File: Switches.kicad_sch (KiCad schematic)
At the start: 31 parts, among them SW4 SW_SPST, SW5 SW_SPST, SW6 SW_SPST, SW7 SW_SPST, SW8 SW_SPST, SW9 SW_SPST, U4 74HC14

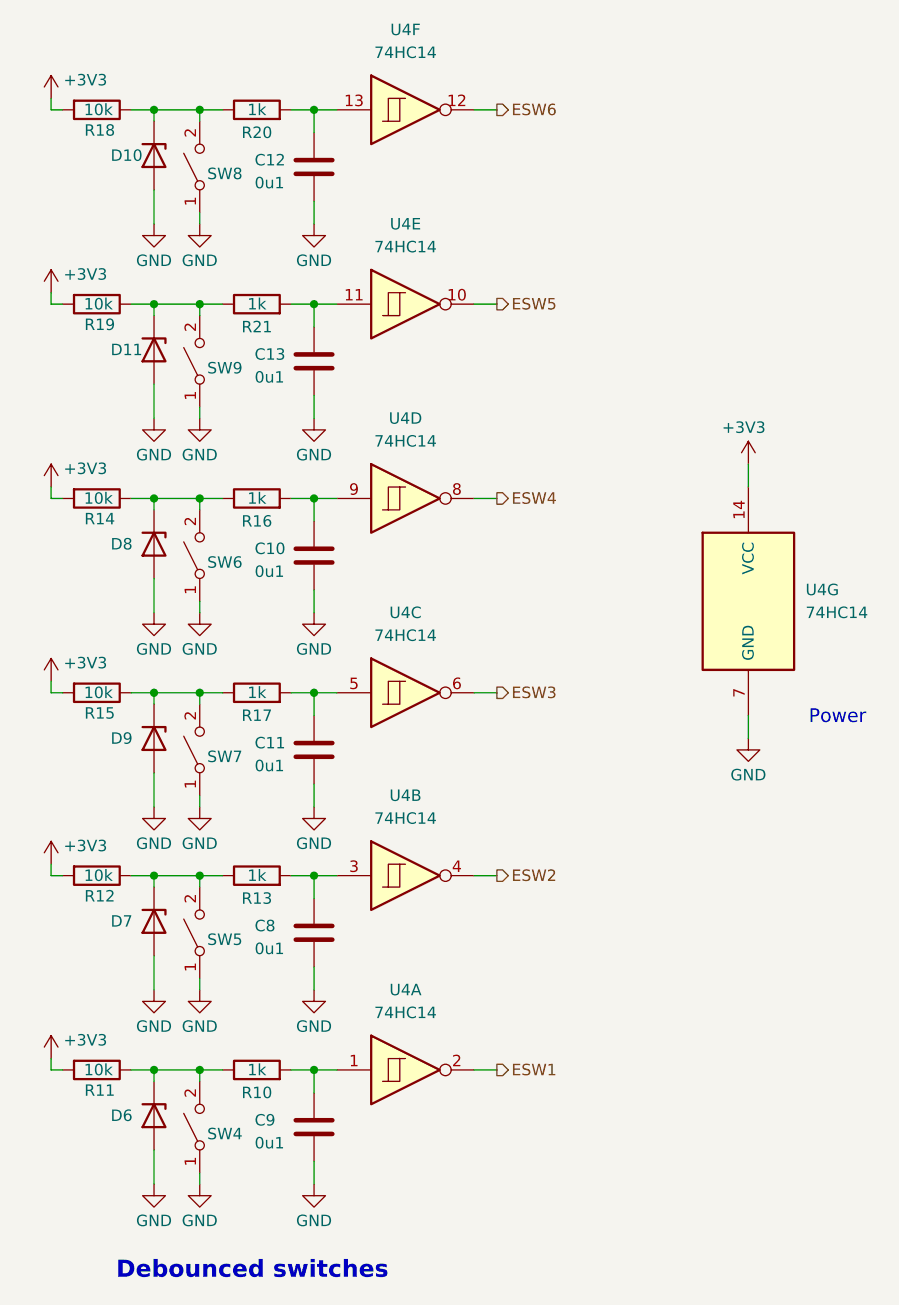
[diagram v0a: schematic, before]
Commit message: schem: add switches footprints
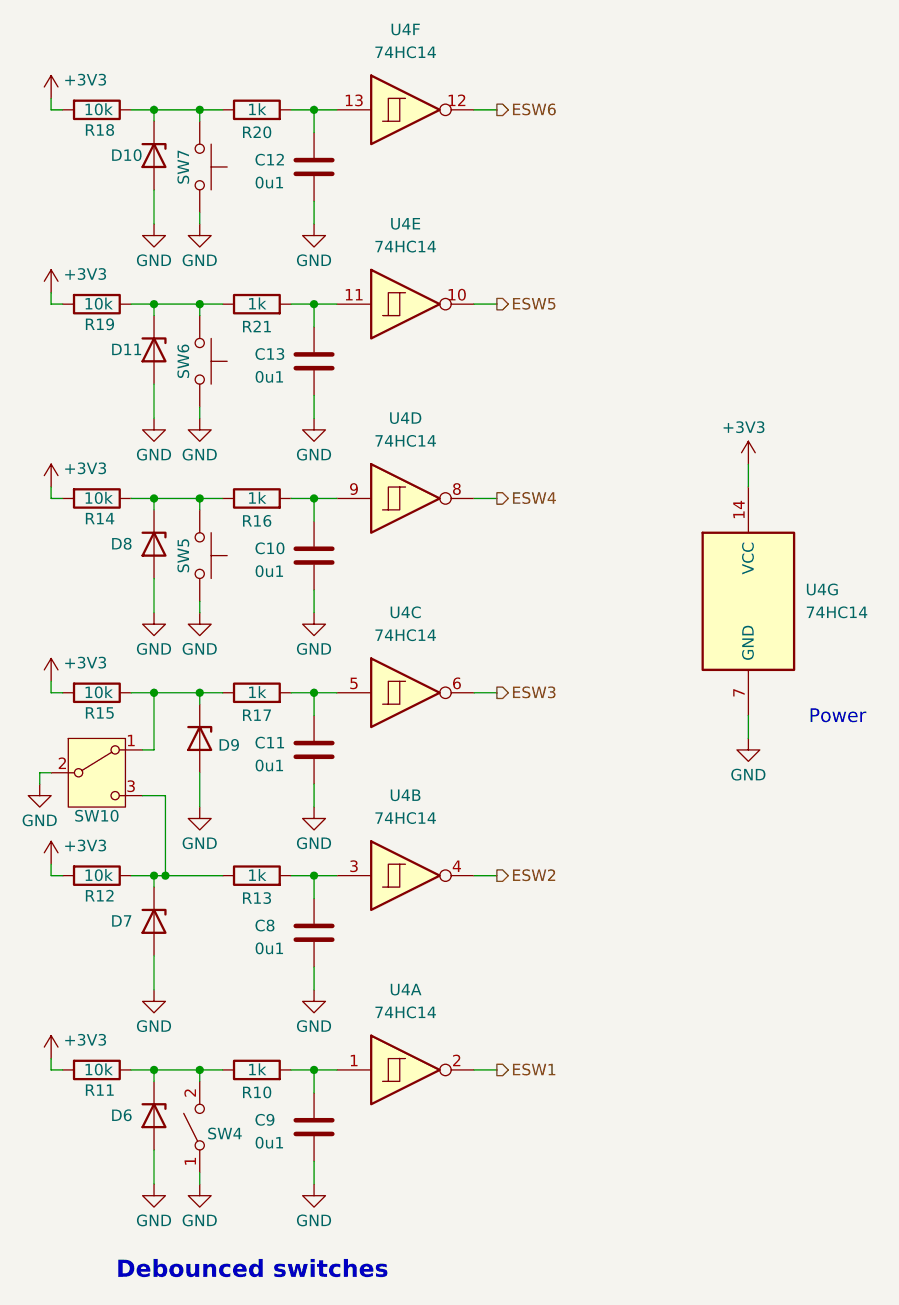
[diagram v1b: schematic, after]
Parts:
- removed SW5, SW6, SW7, SW8, SW9: SW_SPST, symbol Switch:SW_SPST
- added SW10: SW_SPDT, Pers:MT-0-102-A101-M200-RS, symbol Switch:SW_SPDT
- added SW5, SW6, SW7: SW_Push, Button_Switch_SMD:SW_SPST_TS-1088-xR020, symbol Switch:SW_Push
- SW4: footprint (none) -> Connector_PinHeader_2.54mm:PinHeader_1x02_P2.54mm_Vertical; now left out of the parts list
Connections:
- net GND: now also SW10.2 (B), SW5.1, SW6.1, SW7.1
- net at D9.1 (K), R15.1, R17.1: now also SW10.1 (A)
- net at D8.1 (K), R14.1, R16.1: now also SW5.2
- net at D11.1 (K), R19.1, R21.1: now also SW6.2
- net at D7.1 (K), R12.1, R13.1: now also SW10.3 (C)
- net at D10.1 (K), R18.1, R20.1: now also SW7.2
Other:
- moved on the sheet: D9

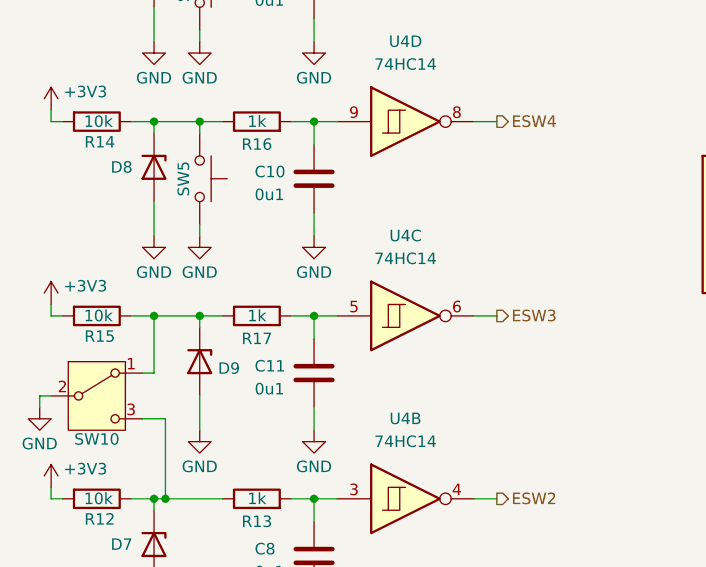
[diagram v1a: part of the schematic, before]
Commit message: schem: add test points
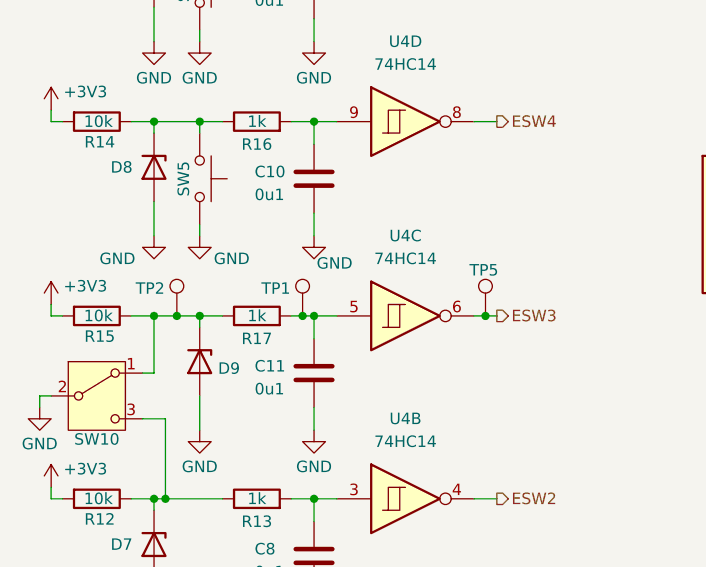
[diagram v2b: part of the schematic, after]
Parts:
- added TP1, TP2, TP5: TestPoint, TestPoint:TestPoint_Pad_D2.0mm, symbol Connector:TestPoint
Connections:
- net ESW3: now also TP5.1
- net at D9.1 (K), R15.1, R17.1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: now also TP2.1
- net at C11.1, R17.2, U4.5: now also TP1.1

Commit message: schem: add title
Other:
- company: (none) -> Valrobotik
- title: (none) -> Carte IHM CDF 1
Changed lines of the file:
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@@
 	(generator_version "9.0")
 	(paper "A4")
+	(title_block
+		(title "Carte IHM CDF 1")
+		(date "2025-11-24")
+		(rev "01")
+		(company "Valrobotik")
+	)
 	(text "Debounced switches"
 		(exclude_from_sim no)

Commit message: schem: reannotate
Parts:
- renumbered C8 to C12, C9 to C13, C12 to C8, C13 to C9, D8 to D12, D7 to D13, D6 to D14, D9 to D15, R18 to R10, R19 to R11, R14 to R12, R15 to R13, R12 to R14, R11 to R15, R20 to R16, R21 to R17, R16 to R18, R17 to R19, R13 to R20, R10 to R21, SW10 to SW4, SW7 to SW5, SW5 to SW7, SW4 to SW8, TP2 to TP5, TP1 to TP6, TP5 to TP7, U4 to U5

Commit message: schem: assign footprints
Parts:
- C10, C11, C12, C13, C8, C9: footprint (none) -> Capacitor_SMD:C_0402_1005Metric
- R10, R11, R12, R13, R14, R15, R16, R17, R18, R19, R20, R21: footprint (none) -> Resistor_SMD:R_0402_1005Metric
- U5: footprint (none) -> Package_SO:SOIC-14_3.9x8.7mm_P1.27mm
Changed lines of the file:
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@@
 			)
 		)
-		(property "Footprint" ""
+		(property "Footprint" "Resistor_SMD:R_0402_1005Metric"
 			(at 119.38 56.642 90)
 			(effects
@@
 			)
 		)
-		(property "Footprint" ""
+		(property "Footprint" "Resistor_SMD:R_0402_1005Metric"
 			(at 119.38 141.732 90)
 			(effects
@@
 			)
 		)
-		(property "Footprint" ""
+		(property "Footprint" "Resistor_SMD:R_0402_1005Metric"
 			(at 137.16 123.698 90)
 			(effects
@@
 			)
 		)
-		(property "Footprint" ""
+		(property "Footprint" "Resistor_SMD:R_0402_1005Metric"
 			(at 137.16 103.378 90)
 			(effects
@@
 			)
 		)
-		(property "Footprint" ""
+		(property "Footprint" "Capacitor_SMD:C_0402_1005Metric"
 			(at 144.4752 46.99 0)
 			(effects
@@
 			)
 		)
-		(property "Footprint" ""
+		(property "Footprint" "Resistor_SMD:R_0402_1005Metric"
 			(at 119.38 120.142 90)
 			(effects
@@
 			)
 		)
-		(property "Footprint" ""
+		(property "Footprint" "Resistor_SMD:R_0402_1005Metric"
 			(at 119.38 35.052 90)
 			(effects
@@
 			)
 		)
-		(property "Footprint" ""
+		(property "Footprint" "Resistor_SMD:R_0402_1005Metric"
 			(at 137.16 81.788 90)
 			(effects
@@
 			)
 		)
-		(property "Footprint" ""
+		(property "Footprint" "Capacitor_SMD:C_0402_1005Metric"
 			(at 144.4752 111.76 0)
 			(effects
@@
 			)
 		)
-		(property "Footprint" ""
+		(property "Footprint" "Package_SO:SOIC-14_3.9x8.7mm_P1.27mm"
 			(at 153.67 143.51 0)
 			(effects
@@
 			)
 		)
-		(property "Footprint" ""
+		(property "Footprint" "Package_SO:SOIC-14_3.9x8.7mm_P1.27mm"
 			(at 191.77 91.44 0)
 			(effects
@@
 			)
 		)
-		(property "Footprint" ""
+		(property "Footprint" "Package_SO:SOIC-14_3.9x8.7mm_P1.27mm"
 			(at 153.67 36.83 0)
 			(effects
@@
 			)
 		)
-		(property "Footprint" ""
+		(property "Footprint" "Package_SO:SOIC-14_3.9x8.7mm_P1.27mm"
 			(at 153.67 80.01 0)
 			(effects
@@
 			)
 		)
-		(property "Footprint" ""
+		(property "Footprint" "Resistor_SMD:R_0402_1005Metric"
 			(at 119.38 99.822 90)
 			(effects
@@
 			)
 		)
-		(property "Footprint" ""
+		(property "Footprint" "Package_SO:SOIC-14_3.9x8.7mm_P1.27mm"
 			(at 153.67 101.6 0)
 			(effects
@@
 			)
 		)
-		(property "Footprint" ""
+		(property "Footprint" "Capacitor_SMD:C_0402_1005Metric"
 			(at 144.4752 90.17 0)
 			(effects
@@
 			)
 		)
-		(property "Footprint" ""
+		(property "Footprint" "Capacitor_SMD:C_0402_1005Metric"
 			(at 144.4752 68.58 0)
 			(effects
@@
 			)
 		)
-		(property "Footprint" ""
+		(property "Footprint" "Capacitor_SMD:C_0402_1005Metric"
 			(at 144.4752 132.08 0)
 			(effects
@@
 			)
 		)
-		(property "Footprint" ""
+		(property "Footprint" "Package_SO:SOIC-14_3.9x8.7mm_P1.27mm"
 			(at 153.67 58.42 0)
 			(effects
@@
 			)
 		)
-		(property "Footprint" ""
+		(property "Footprint" "Resistor_SMD:R_0402_1005Metric"
 			(at 137.16 60.198 90)
 			(effects
@@
 			)
 		)
-		(property "Footprint" ""
+		(property "Footprint" "Resistor_SMD:R_0402_1005Metric"
 			(at 137.16 38.608 90)
 			(effects
@@
 			)
 		)
-		(property "Footprint" ""
+		(property "Footprint" "Resistor_SMD:R_0402_1005Metric"
 			(at 137.16 145.288 90)
 			(effects
@@
 			)
 		)
-		(property "Footprint" ""
+		(property "Footprint" "Package_SO:SOIC-14_3.9x8.7mm_P1.27mm"
 			(at 153.67 121.92 0)
 			(effects
@@
 			)
 		)
-		(property "Footprint" ""
+		(property "Footprint" "Resistor_SMD:R_0402_1005Metric"
 			(at 119.38 78.232 90)
 			(effects
@@
 			)
 		)
-		(property "Footprint" ""
+		(property "Footprint" "Capacitor_SMD:C_0402_1005Metric"
 			(at 144.4752 153.67 0)
 			(effects

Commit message: schem: add part numbers to BOM
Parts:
- C10, C11, C12, C13, C8, C9: Basic (none) -> Y; JLCPCB Part # (none) -> C1525; Manufacturer (none) -> Samsung Electro-Mechanics; Manufacturer Part Number (none) -> CL05B104KO5NNNC
- R10, R11, R12, R13, R14, R15: Basic (none) -> Y; JLCPCB Part # (none) -> C25744; Manufacturer (none) -> Uniroyal Elec; Manufacturer Part Number (none) -> 0402WGF1002TCE
- R16, R17, R18, R19, R20, R21: Basic (none) -> Y; JLCPCB Part # (none) -> C11702; Manufacturer (none) -> Uniroyal Elec; Manufacturer Part Number (none) -> 0402WGF1001TCE
- SW4: now left out of the parts list
- U5: Basic (none) -> Y; JLCPCB Part # (none) -> C5605; Manufacturer (none) -> Nexperia; Manufacturer Part Number (none) -> 74HC14D,653

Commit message: pcb: add layout refinement and board outline
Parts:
- SW5, SW6, SW7: footprint Button_Switch_SMD:SW_SPST_TS-1088-xR020 -> Button_Switch_THT:SW_PUSH_6mm_H7.3mm; Basic Y -> (none); JLCPCB Part # C720477 -> (none); Manufacturer XUNPU -> (none); Manufacturer Part Number TS-1088-AR02016 -> (none); now left out of the parts list
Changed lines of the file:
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@@
 		(unit 1)
 		(exclude_from_sim no)
-		(in_bom yes)
+		(in_bom no)
 		(on_board yes)
 		(dnp no)
@@
 			)
 		)
-		(property "Footprint" "Button_Switch_SMD:SW_SPST_TS-1088-xR020"
+		(property "Footprint" "Button_Switch_THT:SW_PUSH_6mm_H7.3mm"
 			(at 135.89 86.36 0)
 			(effects
@@
 			)
 		)
-		(property "Manufacturer" "XUNPU"
+		(property "Manufacturer" ""
 			(at 130.81 86.36 0)
 			(effects
@@
 			)
 		)
-		(property "Manufacturer Part Number" "TS-1088-AR02016"
+		(property "Manufacturer Part Number" ""
 			(at 130.81 86.36 0)
 			(effects
@@
 			)
 		)
-		(property "Basic" "Y"
+		(property "Basic" ""
 			(at 130.81 86.36 0)
 			(effects
@@
 			)
 		)
-		(property "JLCPCB Part #" "C720477"
+		(property "JLCPCB Part #" ""
 			(at 130.81 86.36 0)
 			(effects
@@
 		(unit 1)
 		(exclude_from_sim no)
-		(in_bom yes)
+		(in_bom no)
 		(on_board yes)
 		(dnp no)
@@
 			)
 		)
-		(property "Footprint" "Button_Switch_SMD:SW_SPST_TS-1088-xR020"
+		(property "Footprint" "Button_Switch_THT:SW_PUSH_6mm_H7.3mm"
 			(at 135.89 43.18 0)
 			(effects
@@
 			)
 		)
-		(property "Manufacturer" "XUNPU"
+		(property "Manufacturer" ""
 			(at 130.81 43.18 0)
 			(effects
@@
 			)
 		)
-		(property "Manufacturer Part Number" "TS-1088-AR02016"
+		(property "Manufacturer Part Number" ""
 			(at 130.81 43.18 0)
 			(effects
@@
 			)
 		)
-		(property "Basic" "Y"
+		(property "Basic" ""
 			(at 130.81 43.18 0)
 			(effects
@@
 			)
 		)
-		(property "JLCPCB Part #" "C720477"
+		(property "JLCPCB Part #" ""
 			(at 130.81 43.18 0)
 			(effects
@@
 		(unit 1)
 		(exclude_from_sim no)
-		(in_bom yes)
+		(in_bom no)
 		(on_board yes)
 		(dnp no)
@@
 			)
 		)
-		(property "Footprint" "Button_Switch_SMD:SW_SPST_TS-1088-xR020"
+		(property "Footprint" "Button_Switch_THT:SW_PUSH_6mm_H7.3mm"
 			(at 135.89 64.77 0)
 			(effects
@@
 			)
 		)
-		(property "Manufacturer" "XUNPU"
+		(property "Manufacturer" ""
 			(at 130.81 64.77 0)
 			(effects
@@
 			)
 		)
-		(property "Manufacturer Part Number" "TS-1088-AR02016"
+		(property "Manufacturer Part Number" ""
 			(at 130.81 64.77 0)
 			(effects
@@
 			)
 		)
-		(property "Basic" "Y"
+		(property "Basic" ""
 			(at 130.81 64.77 0)
 			(effects
@@
 			)
 		)
-		(property "JLCPCB Part #" "C720477"
+		(property "JLCPCB Part #" ""
 			(at 130.81 64.77 0)
 			(effects

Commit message: pcb: refine layout
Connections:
- net ESW2: now also U5.6; no longer U5.4
- net ESW3: now also U5.4; no longer U5.6
- net at C11.1, R19.2, TP6.1: now also U5.3; no longer U5.5
- net at C12.1, R20.2: now also U5.5; no longer U5.3
